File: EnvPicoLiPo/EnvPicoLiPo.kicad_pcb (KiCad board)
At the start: 2 copper layers, 21.1 x 58.1 mm, 67 parts, among them J2 SKRKAEE020, J3 2.54mm header 01x20, J4 2.54mm header 01x20, J5 Conn_01x03_Male, U1 LM3671MF 3.3, U2 BQ24072RGT, U3 RP2040, U4 ESP32-PICO-D4, X1 XO 32 12Mhz 3225 seiko

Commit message: some useful updates
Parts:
- moved R6 1.37 mm to (103.1, 66.1), turned to 180 degrees
- moved C23 1.32 mm to (102.6, 97.9)
- moved C22 0.70 mm to (104.4, 107.3)
- moved C20 0.68 mm to (110.5, 68.4), turned to -90 degrees
- moved C24 0.48 mm to (99.1, 108.3)
- moved C25 0.46 mm to (97.0, 104.1), turned to 0 degrees
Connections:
- net /~USB_BOOT renamed /~{USB_BOOT}
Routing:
- net +3V3: track 112.8 -> 78.4 mm, vias 8 -> 13
- net ESP_CS: track 27.5 -> 32.2 mm
- net Net-(C25-Pad2): track 5.98 -> 4.50 mm
- net Net-(C20-Pad2): track 7.93 -> 8.96 mm
- net Net-(L2-Pad1): track 3.09 -> 2.99 mm, vias 2 -> 0
- net GND: vias 31 -> 33
- added copper zone on B.Cu, net +3V3
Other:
- board size 21.1 x 58.1 mm -> 21.2 x 58.1 mm
- net class Default removed
- net class USB_DIFF_90 removed
- board text added: "EnvOpenPico BLE/WiFi/Battery"

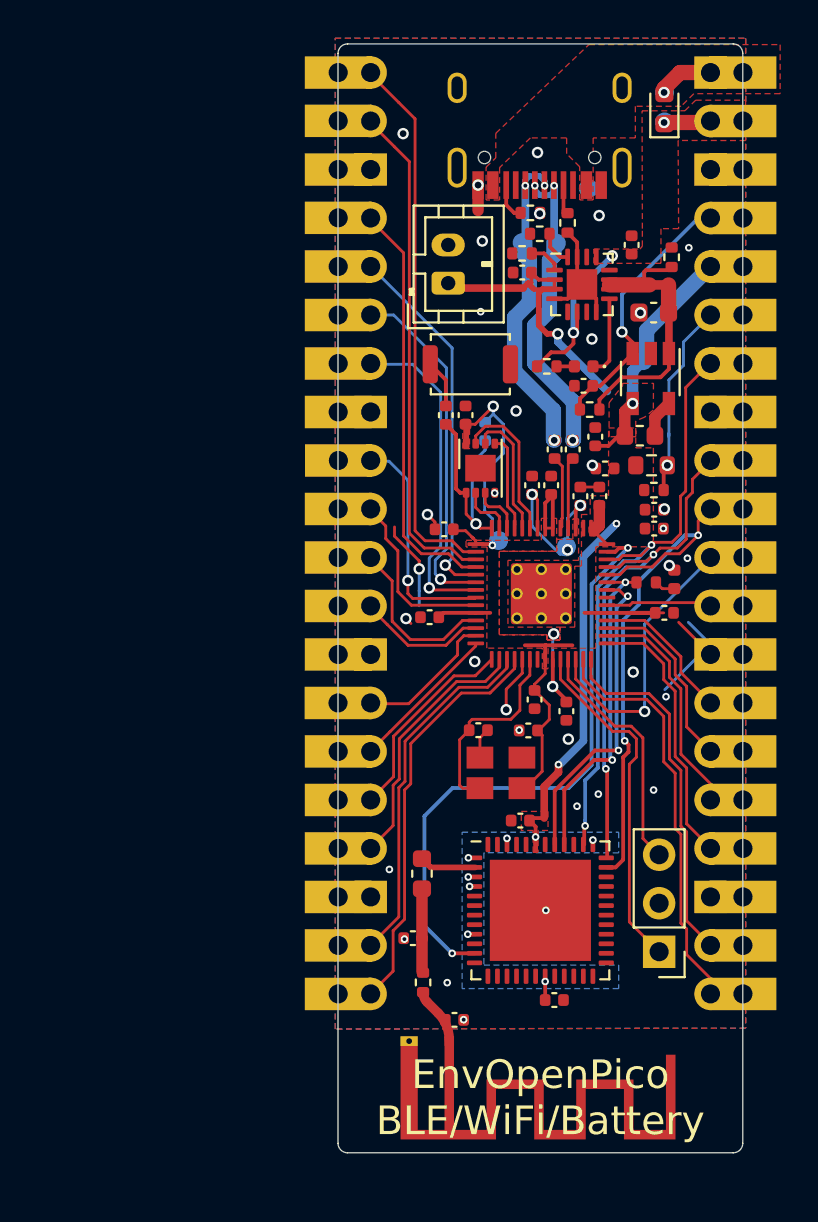
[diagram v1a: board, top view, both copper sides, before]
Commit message: Corrected all the via placements so they dont cause issues and removed some redundant parts
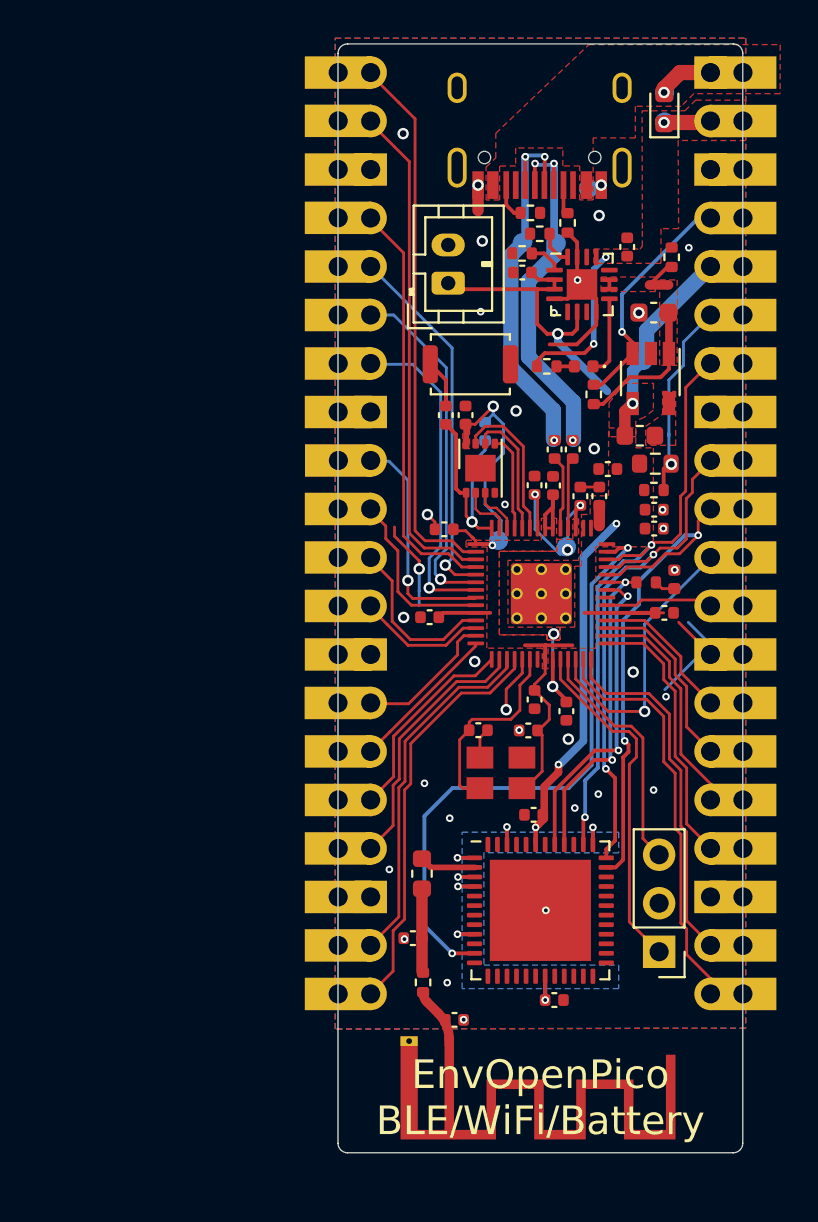
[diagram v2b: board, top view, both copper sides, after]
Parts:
- removed C12: 0.1uf 0402, Capacitor_SMD:C_0402_1005Metric
- removed C4: 1uf 0402, Capacitor_SMD:C_0402_1005Metric
- D4: value Schottky 0603 -> 1n4002 0603
- R7: value 100ohm -> 100k 0402
- moved C9 1.82 mm to (107.2, 79.5), turned to 180 degrees
- moved R7 0.82 mm to (106.4, 75.6), turned to 90 degrees
- moved C23 0.76 mm to (103.3, 97.6)
- moved C19 0.26 mm to (108.2, 67.9)
- moved R9 0.22 mm to (109.7, 79.2)
- moved C7 0.13 mm to (103.3, 80.3)
- moved C8 0.10 mm to (104.3, 80.4)
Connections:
- BT1 pad 1: Net-(BT1-Pad1) -> VBAT
- C21 pad 2: Net-(BT1-Pad1) -> VBAT
- U2 pad 2: Net-(BT1-Pad1) -> VBAT
- U2 pad 3: Net-(BT1-Pad1) -> VBAT
- U2 pad 6: VSYS -> VBAT
- U2 pad 7: Net-(D1-Pad1) -> (no net)
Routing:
- net VBAT: track 0.00 -> 17.1 mm, vias 0 -> 1
- net Net-(BT1-Pad1): track 16.4 -> 0.00 mm, vias 1 -> 0
- net +3V3: track 78.4 -> 88.1 mm
- net Net-(C20-Pad2): track 8.96 -> 2.28 mm
- net USB_D+: track 16.4 -> 20.3 mm
- net GND: track 27.6 -> 30.8 mm, vias 33 -> 35
- net USB_D-: track 16.3 -> 19.5 mm
- net Net-(L1-Pad1): track 1.99 -> 0.00 mm
- net 3V3_EN: track 14.7 -> 12.9 mm
- net VDD: track 9.27 -> 7.67 mm
- net VSYS: track 12.6 -> 11.9 mm
- net (no net): vias 1 -> 0
- added copper zone on F.Cu, net Net-(C20-Pad2)
- added copper zone on F.Cu, net Net-(L1-Pad1)
- added copper zone on F.Cu, net VDD
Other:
- board text added: "DNF"

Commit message: removed ESP32 and wifi bits for now, will re-add something later on with further testing.
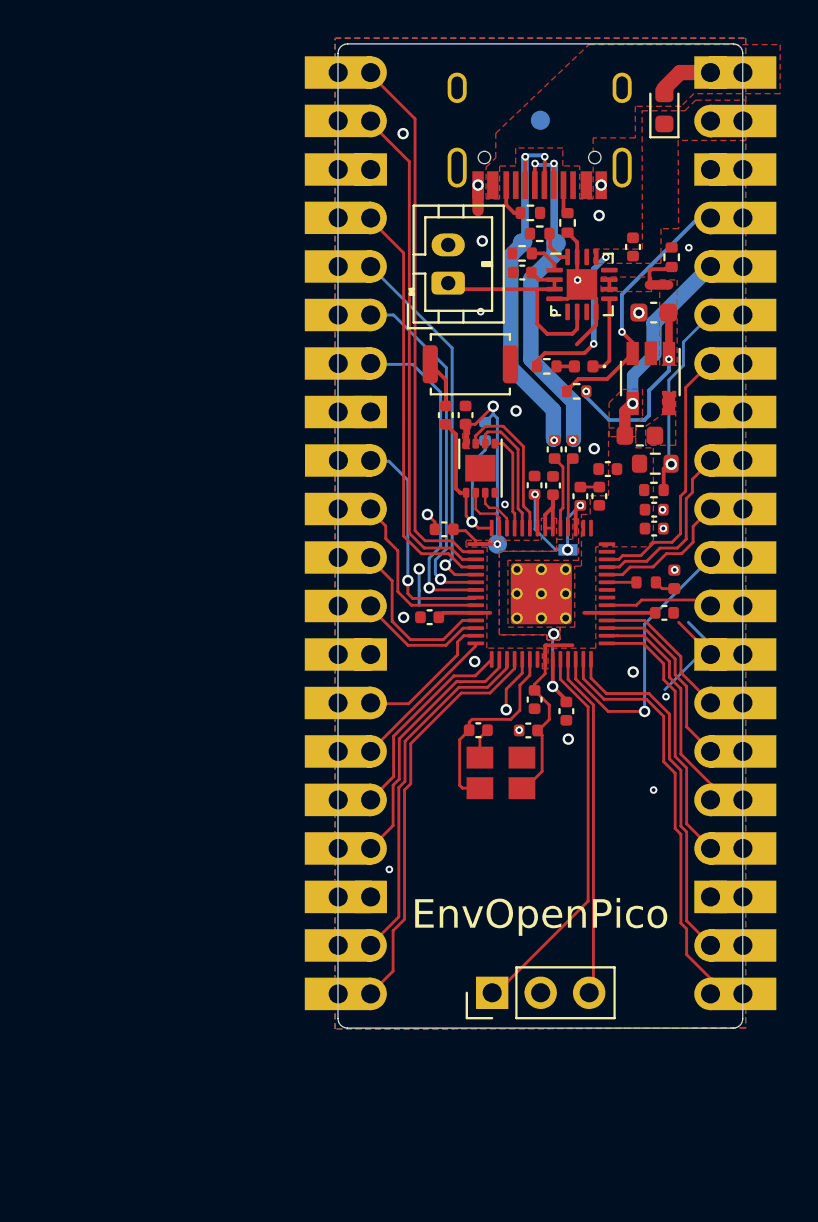
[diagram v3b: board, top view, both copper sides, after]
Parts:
- removed AE1: Antenna, RF_Antenna:Texas_SWRA117D_2.4GHz_Left
- removed C22: 4.7uF 0402, Capacitor_SMD:C_0402_1005Metric
- removed C23: 0402 1uF, Capacitor_SMD:C_0402_1005Metric
- removed C24: 0402 1.5pF, Capacitor_SMD:C_0402_1005Metric
- removed C25: 0402 1pF, Capacitor_SMD:C_0402_1005Metric
- removed L2: 3.9nH 0603, Inductor_SMD:L_0603_1608Metric
- removed R15: 0402 0R, Resistor_SMD:R_0402_1005Metric
- removed TP4, TP5, TP6: TestPoint, TestPoint:TestPoint_Pad_D1.0mm
- removed U4: ESP32-PICO-D4, Package_DFN_QFN:QFN-48-1EP_7x7mm_P0.5mm_EP5.3x5.3mm
- moved J5 9.01 mm to (101.1, 106.9), turned to 90 degrees
- moved TP3 4.37 mm to (103.6, 61.2)
- moved R7 0.91 mm to (105.5, 75.4), turned to 180 degrees
- moved C19 0.30 mm to (108.5, 67.9)
- moved TP8 0.20 mm to (101.4, 83.4)
- moved TP7 0.18 mm to (105.1, 83.7)
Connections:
- net ESP_CLK renamed /GPIO26_ADC0
- net ESP_MISO renamed /GPIO28_ADC2
- net ESP_MOSI renamed /GPIO27_ADC1
- net U-RXD renamed /GPIO25
- FLASH1 pad 9: (no net) -> unconnected-(FLASH1-Pad9)
- U2 pad 12: (no net) -> unconnected-(U2-Pad12)
- U2 pad 14: (no net) -> unconnected-(U2-Pad14)
- U2 pad 7: (no net) -> unconnected-(U2-Pad7)
- U3 pad 21: (no net) -> /XOUT
- U3 pad 35: (no net) -> /GPIO23
- U3 pad 36: U-TXD -> /GPIO24
- U3 pad 41: ESP_CS -> /GPIO29_ADC3
- X1 pad 1: (no net) -> unconnected-(X1-Pad1)
- e1 pad 3: (no net) -> unconnected-(e1-Pad3)
- e1 pad 9: (no net) -> unconnected-(e1-Pad9)
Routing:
- net +3V3: track 88.1 -> 46.3 mm, vias 13 -> 3
- net ESP_CS: track 32.2 -> 0.00 mm, vias 2 -> 0
- net /GPIO26_ADC0: track 27.5 -> 7.33 mm, vias 2 -> 0
- net /GPIO27_ADC1: track 27.3 -> 9.42 mm, vias 2 -> 0
- net /GPIO28_ADC2: track 31.5 -> 14.0 mm, vias 2 -> 0
- net U-TXD: track 16.6 -> 0.00 mm, vias 2 -> 0
- net /GPIO25: track 17.0 -> 1.31 mm, vias 2 -> 0
- net GND: track 30.8 -> 24.8 mm, vias 35 -> 27
- net /SWD: track 12.7 -> 17.8 mm
- net VBAT: track 17.1 -> 12.2 mm, vias 1 -> 0
- net Net-(C25-Pad2): track 4.50 -> 0.00 mm
- net VSYS: track 11.9 -> 8.44 mm, vias 3 -> 2
- net Net-(AE1-Pad1): track 3.00 -> 0.00 mm
- net Net-(L2-Pad1): track 2.99 -> 0.00 mm
- net VDD: track 7.67 -> 9.98 mm, vias 0 -> 2
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- removed copper zone on B.Cu, net +3V3
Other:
- board size 21.2 x 58.1 mm -> 21.2 x 51.6 mm
- board text added: "1.1V"
- board text added: "3.3V"
- board text added: "EnvOpenPico"
- board text added: "GND"
- board text removed: "0.09mm width difference is needed for ground plane coverage"
- board text removed: "DO NOT CHANGE THE SIZE OF THE PCB OR THE PINOUT"
- board text removed: "EnvOpenPico BLE/WiFi/Battery"
- board text removed: "If you replace components with smaller versions please ensure they are avalibale via JLCPCB for SMD installation"

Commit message: moved the battery connector to the bottom of the board and rotated the debug header 90 degrees to fit along side.
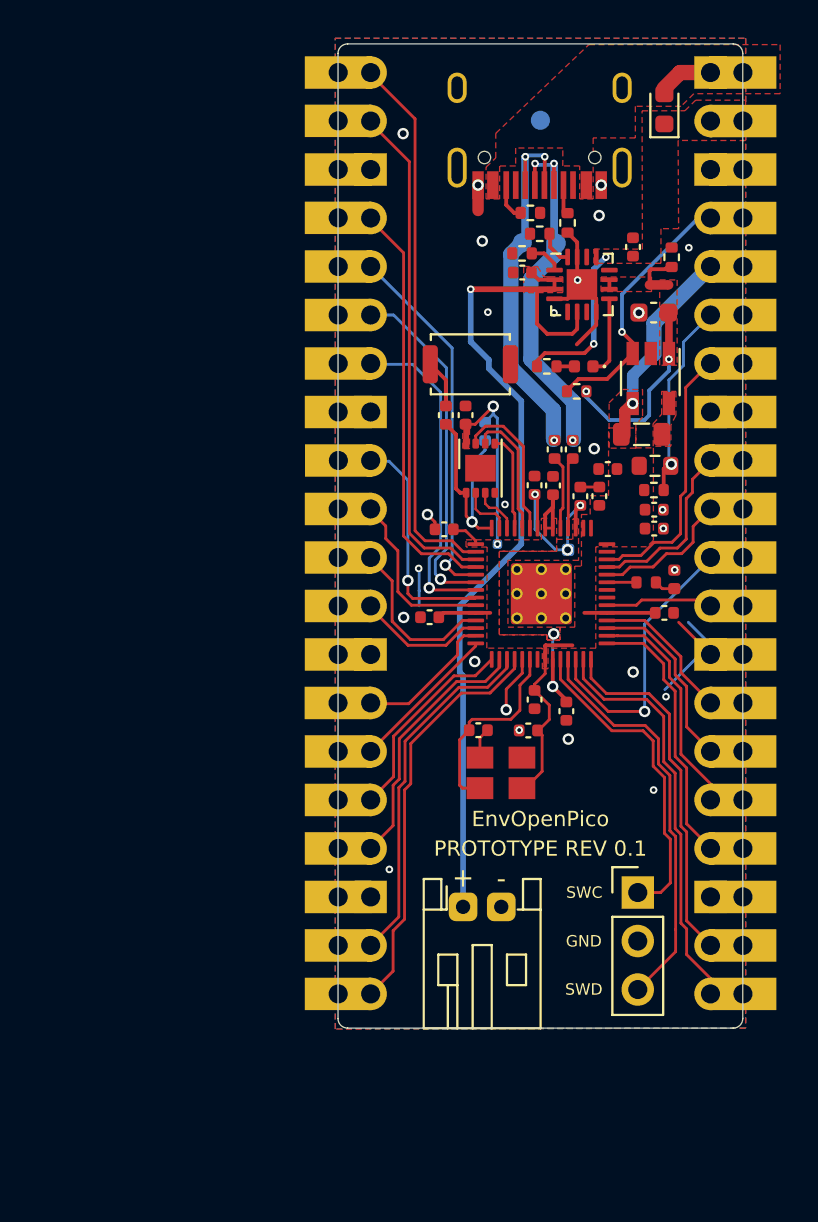
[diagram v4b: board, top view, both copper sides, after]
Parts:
- removed G***: LOGO, EnvExtras:logo
- BT1: footprint Connector_JST:JST_PH_B2B-PH-K_1x02_P2.00mm_Vertical -> Connector_JST:JST_PH_S2B-PH-K_1x02_P2.00mm_Horizontal
- L1: value INDUCTOR 2.2uH 0603 -> INDUCTOR 2.2uH 0805; footprint Inductor_SMD:L_0603_1608Metric -> Inductor_SMD:L_0805_2012Metric
- moved BT1 32.7 mm to (99.6, 102.4), turned to 0 degrees
- moved J5 9.26 mm to (108.7, 101.7), turned to 0 degrees
- moved L1 0.12 mm to (108.9, 77.7)
- moved R9 0.11 mm to (109.6, 79.3)
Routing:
- net VBAT: track 12.2 -> 47.1 mm, vias 0 -> 1
- net /SWD: track 17.8 -> 21.4 mm
- net /SWCLK: track 20.1 -> 17.0 mm
- net +3V3: track 46.3 -> 44.7 mm
- net GND: vias 27 -> 26
- added copper zone on F.Cu, net VBAT
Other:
- board text added: "+"
- board text added: "-"
- board text added: "PROTOTYPE REV 0.1"
- board text added: "SWC"
- board text added: "SWD"
- board text added: "https://github.com/Envious-Data/EnvOpenPico"

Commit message: changed JST connector for more common type, adjusted some parts to do with flash
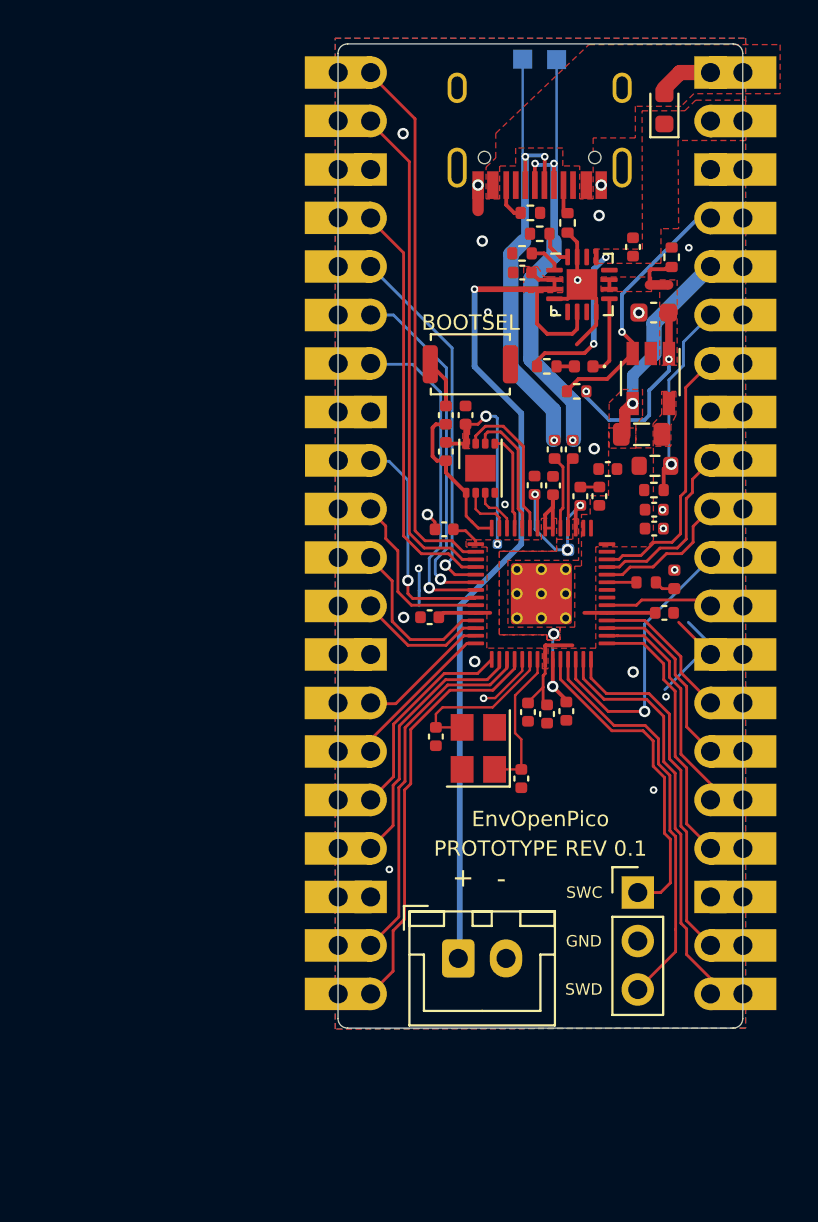
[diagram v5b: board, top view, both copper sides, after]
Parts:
- removed the C2 at (100.4, 93.2)
- removed TP3: TestPoint, TestPoint:TestPoint_Pad_D1.0mm
- removed X1: XO 32 12Mhz 3225 seiko, Crystal:Crystal_SMD_SeikoEpson_TSX3225-4Pin_3.2x2.5mm
- added C18: 15pf 0402, Capacitor_SMD:C_0402_1005Metric, F.Cu at (98.2, 93.5)
- added C19: 15pf 0402, Capacitor_SMD:C_0402_1005Metric, F.Cu at (102.6, 95.7)
- added Y1: Crystal_GND24 12MHz, Crystal:Crystal_SMD_3225-4Pin_3.2x2.5mm, F.Cu at (100.4, 94.1)
- BT1: footprint Connector_JST:JST_PH_S2B-PH-K_1x02_P2.00mm_Horizontal -> Connector_JST:JST_XH_B2B-XH-A_1x02_P2.50mm_Vertical
- R11: renamed from R2; value DNF -> 10K 0402; moved to F.Cu
- moved TP2 9.61 mm to (104.5, 58.0)
- moved TP1 9.61 mm to (102.7, 58.0)
- moved BT1 2.71 mm to (99.3, 105.1)
- moved R11 2.31 mm to (98.7, 78.6)
- moved C11 1.00 mm to (104.0, 92.3)
- moved C12 0.96 mm to (103.0, 92.2), turned to -90 degrees
- renumbered C19 to C1, C13 to C10, C14 to C11, C15 to C12, C16 to C13, C18 to C14, C10 to C15, C3 to C16, C5 to C17, C20 to C2, C17 to C20, C1 to C3, C21 to C4, C9 to C5, C11 to C8, C8 to C9, D4 to D1, J2 to J1, J3 to J2, J4 to J3, J5 to J4, R5 to R1, R4 to R10, R1 to R12, R8 to R13, R12 to R2, R6 to R3, R7 to R4, R9 to R5, R14 to R6, R11 to R7, R10 to R8, R3 to R9, TP7 to TP6, U2 to U1, U1 to U2
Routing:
- net /XOUT: track 0.00 -> 7.78 mm
- net USB_D-: track 19.2 -> 24.7 mm
- net USB_D+: track 20.0 -> 25.2 mm
- net +3V3: track 44.7 -> 40.2 mm
- net /QSPI_SS: track 11.6 -> 8.00 mm, vias 1 -> 0
- net VBAT: track 47.1 -> 49.5 mm
- net /XIN: track 10.5 -> 8.52 mm
- net GND: track 24.8 -> 23.4 mm, vias 26 -> 24
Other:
- board text added: "BOOTSEL"
